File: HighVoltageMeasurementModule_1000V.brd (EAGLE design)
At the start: 48 x 24 mm, 8 parts

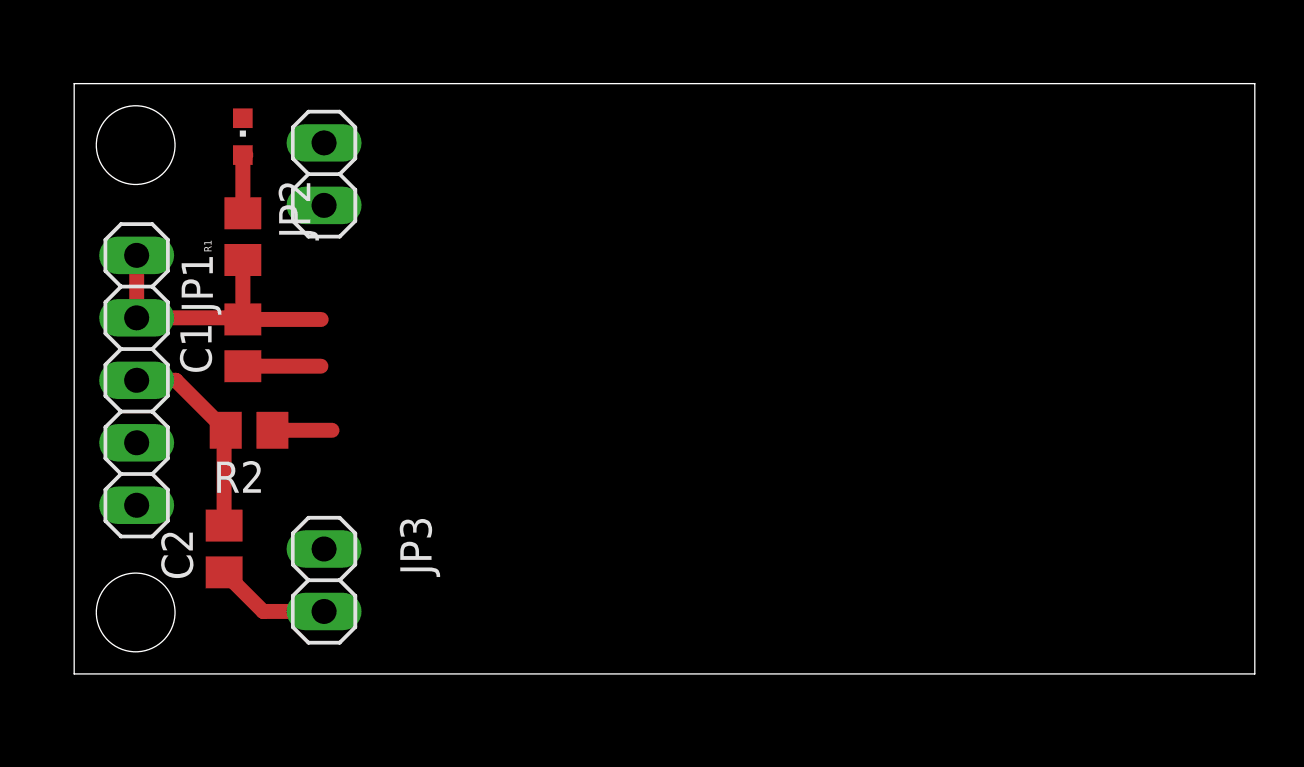
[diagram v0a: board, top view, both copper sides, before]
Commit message: voltage module layouted
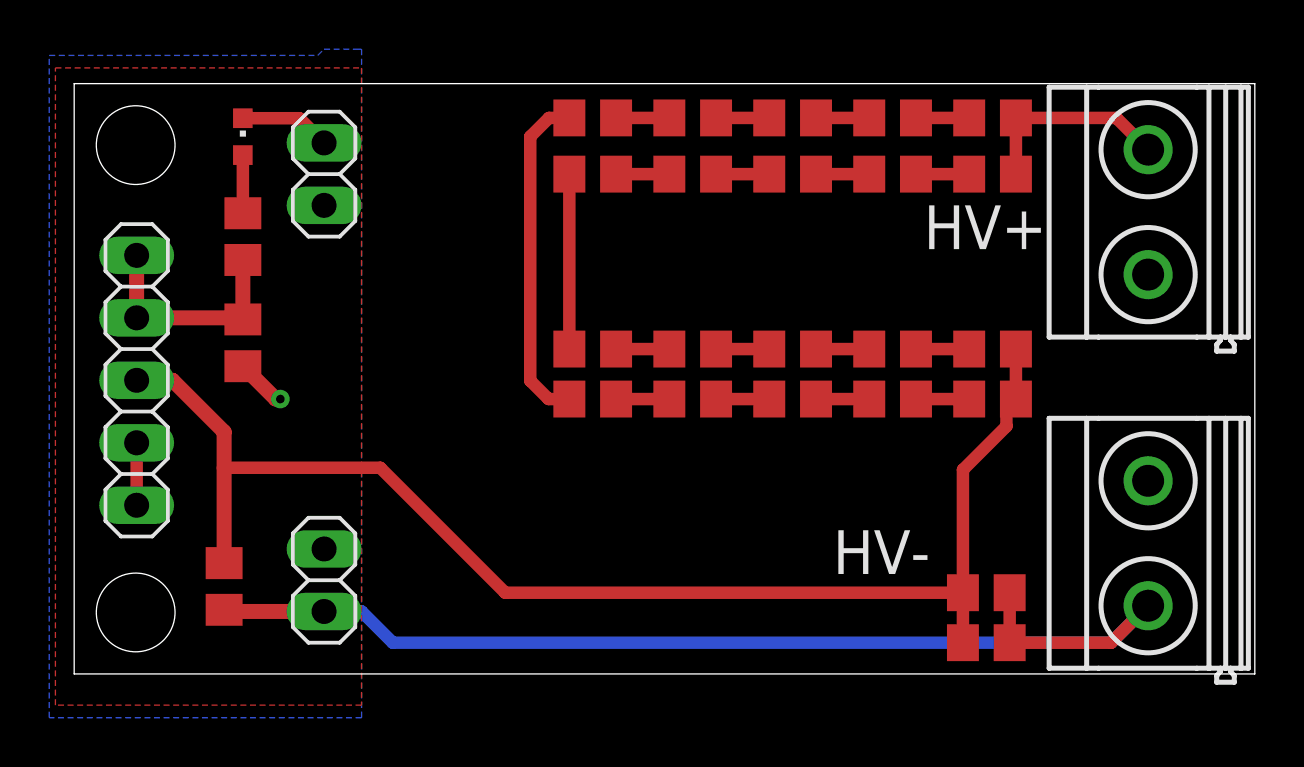
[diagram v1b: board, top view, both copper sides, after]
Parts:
- added R10, R11, R12, R13, R14, R18, R23, R28, R3, R33, R38, R4, R43, R45, R5, R6, R7, R8, R9: 200k, rcl:R0805
- added R15, R53: 10k, rcl:R0805
- added X1, X2: MKDSN1,5/2-5,08, con-phoenix-508:MKDSN1,5/2-5,08
- R2: value 10k -> 200k
- moved R2 32.0 mm to (37.3, 20.3)
- moved C2 1.52 mm to (6.10, 3.56)
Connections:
- removed net N$6: C2.2, JP1.3, R2.2
- new net HV+: R2.1, R3.1, X1.2
- new net N$10: R10.1, R9.2
- new net N$11: R10.2, R11.1
- new net N$12: R11.2, R12.1
- new net N$13: R12.2, R14.1
- new net N$14: R13.2, R18.1
- new net N$15: C2.2, JP1.3, R14.2, R15.2, R45.2, R53.2
- new net N$19: R18.2, R23.1
- new net N$2: R4.2, R5.1
- new net N$24: R23.2, R28.1
- new net N$29: R28.2, R33.1
- new net N$3: R5.2, R6.1
- new net N$34: R33.2, R38.1
- new net N$39: R38.2, R43.1
- new net N$4: R6.2, R7.1
- new net N$41: R43.2, R45.1
- new net N$7: R7.2, R9.1
- new net N$8: R3.2, R8.1
- new net N$9: R13.1, R8.2
- net GND: now also R15.1, R53.1, X2.1
- net N$1: now also R2.2, R4.1; no longer R2.1
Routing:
- net N$15: track 0.00 -> 54.7 mm
- net GND: track 7.89 -> 55.4 mm, vias 0 -> 1
- net N$24: track 0.00 -> 13.7 mm
- net N$6: track 8.37 -> 0.00 mm
- net HV+: track 0.00 -> 8.20 mm
- net N$7: track 0.00 -> 7.11 mm
- net 5VDC: track 12.5 -> 9.30 mm
- net N$8: track 0.00 -> 2.16 mm
- net N$41: track 0.00 -> 2.16 mm
- net N$4: track 0.00 -> 2.16 mm
- net N$34: track 0.00 -> 2.16 mm
- net N$3: track 0.00 -> 2.16 mm
- net N$29: track 0.00 -> 2.16 mm
- net N$19: track 0.00 -> 2.16 mm
- net N$14: track 0.00 -> 2.16 mm
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- added copper zone on layer 1, net GND
- added copper zone on layer 16, net GND
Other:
- board text added: "HV+"
- board text added: "HV-"

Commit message: voltage module layout changed
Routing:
- net GND: vias 1 -> 5
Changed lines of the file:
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@@
 <layer number="14" name="Route14" color="22" fill="1" visible="no" active="no"/>
 <layer number="15" name="Route15" color="23" fill="1" visible="no" active="no"/>
-<layer number="16" name="Bottom" color="1" fill="1" visible="yes" active="yes"/>
+<layer number="16" name="Bottom" color="1" fill="1" visible="no" active="yes"/>
 <layer number="17" name="Pads" color="2" fill="1" visible="yes" active="yes"/>
 <layer number="18" name="Vias" color="2" fill="1" visible="yes" active="yes"/>
@@
 <wire x1="11.684" y1="2.54" x2="10.16" y2="2.54" width="0.508" layer="16"/>
 <wire x1="12.954" y1="1.27" x2="11.684" y2="2.54" width="0.508" layer="16"/>
+<via x="9.906" y="14.478" extent="1-16" drill="0.35"/>
+<via x="10.414" y="12.446" extent="1-16" drill="0.35"/>
+<via x="4.318" y="19.05" extent="1-16" drill="0.35"/>
+<via x="1.27" y="5.08" extent="1-16" drill="0.35"/>
 </signal>
 <signal name="HV+">
